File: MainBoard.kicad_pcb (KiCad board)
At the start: 2 copper layers, 120 x 68 mm, 89 parts, among them J1 DB25, P1 BOOT, P10 CONN_01X03, P11 CONN_01X03, P12 CONN_01X03, P13 CONN_01X03, P14 CONN_01X02, P15 CONN_02X07, P16 CONN_02X04, P18 CONN_01X03, P2 CONN_01X04, P3 CONN_02X04, P4 HOLE, P5 HOLE, P6 HOLE, P7 HOLE, P8 CONN_01X02, P9 CONN_01X03, Q1 BSS138, Q2 BSS138, Q3 DMN65D8L, SW1 RESET, U1 mp2307, U10 SI4425DDY, U11 INA199A2, U12 ADS1015, U2 DYS_mini_ESC, U3 DYS_mini_ESC, U4 DYS_mini_ESC, U5 DYS_mini_ESC, U6 TLV1117LV33, U7 TENDA_P200, U8 pca9685, U9 STM32F103CBT6, Y1 8MHz

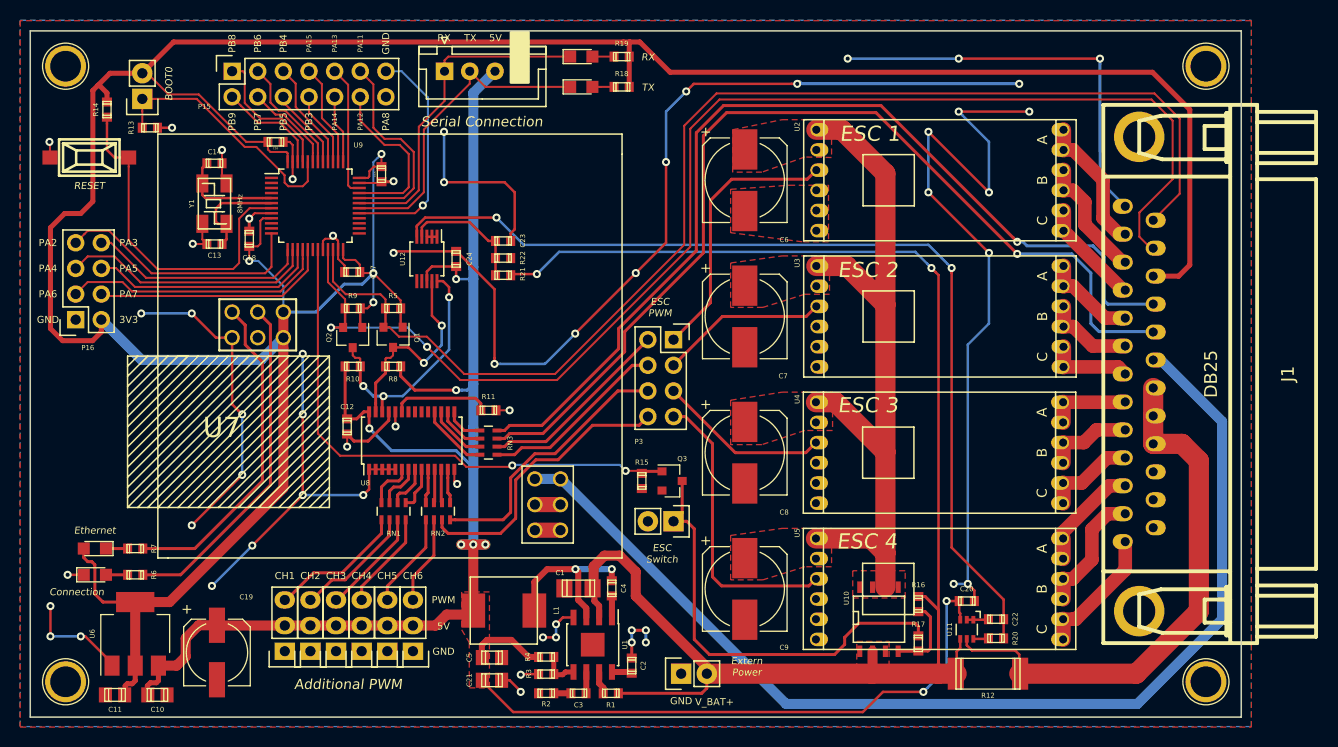
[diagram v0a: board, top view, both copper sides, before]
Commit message: Fix ina199a2 routing
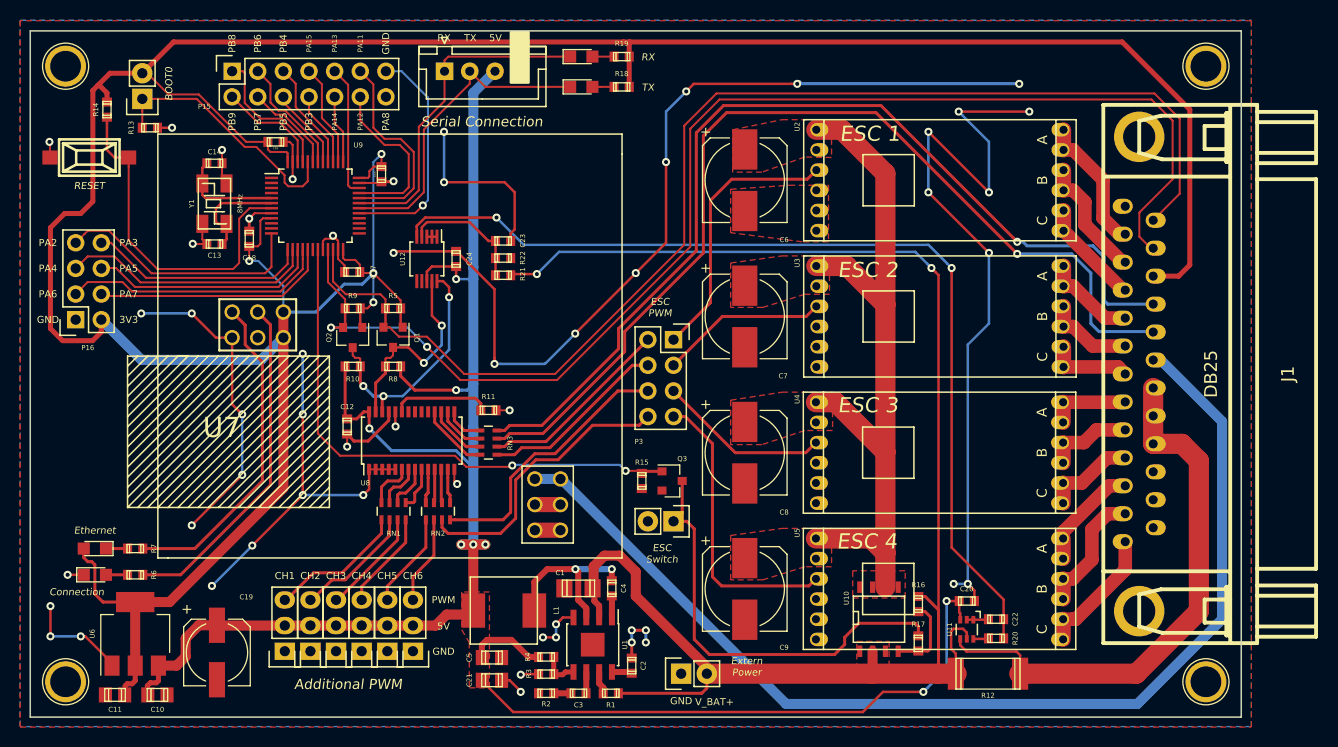
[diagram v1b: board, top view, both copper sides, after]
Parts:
- R21: value 30.1k %1 -> 30.1k 1%
- R3: value 10k 1% -> 10k %1
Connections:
- U11 pad 4: /V_BAT -> /V_IN
- U11 pad 5: /V_IN -> /V_BAT
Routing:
- net GND: track 401.5 -> 351.6 mm, vias 57 -> 54
- net /V_BAT: track 151.0 -> 154.2 mm
- net /V_IN: track 54.1 -> 54.8 mm
